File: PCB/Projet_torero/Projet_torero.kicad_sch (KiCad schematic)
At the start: 0 parts

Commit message: Add files via upload
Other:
- added sheet ALIMENTATION (Alimentation.kicad_sch)
- sheet PUISSANCE ports: added FWDD, FWDG, REVD, REVG, V7.2; removed none
- sheet STM32 ports: added FWDD, FWDG, REVD, REVG; removed none
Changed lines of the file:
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@@
 	(generator_version "8.0")
 	(paper "A4")
+	(wire
+		(pts
+			(xy 129.54 63.5) (xy 140.97 63.5)
+		)
+		(stroke
+			(width 0)
+			(type default)
+		)
+	)
+	(wire
+		(pts
+			(xy 129.54 55.88) (xy 140.97 55.88)
+		)
+		(stroke
+			(width 0)
+			(type default)
+		)
+	)
+	(wire
+		(pts
+			(xy 129.54 58.42) (xy 140.97 58.42)
+		)
+		(stroke
+			(width 0)
+			(type default)
+		)
+	)
+	(wire
+		(pts
+			(xy 129.54 60.96) (xy 140.97 60.96)
+		)
+		(stroke
+			(width 0)
+			(type default)
+		)
+	)
 	(sheet
 		(at 22.86 114.3)
@@
 			)
 		)
+		(pin "FWDG" input
+			(at 129.54 55.88 0)
+			(effects
+				(font
+					(size 1.27 1.27)
+				)
+				(justify right)
+			)
+		)
+		(pin "REVG" input
+			(at 129.54 58.42 0)
+			(effects
+				(font
+					(size 1.27 1.27)
+				)
+				(justify right)
+			)
+		)
+		(pin "FWDD" input
+			(at 129.54 60.96 0)
+			(effects
+				(font
+					(size 1.27 1.27)
+				)
+				(justify right)
+			)
+		)
+		(pin "REVD" input
+			(at 129.54 63.5 0)
+			(effects
+				(font
+					(size 1.27 1.27)
+				)
+				(justify right)
+			)
+		)
 		(instances
 			(project "Projet_torero"
@@
 	)
 	(sheet
+		(at 176.53 113.03)
+		(size 83.82 41.91)
+		(fields_autoplaced yes)
+		(stroke
+			(width 0.1524)
+			(type solid)
+		)
+		(fill
+			(color 0 0 0 0.0000)
+		)
+		(property "Sheetname" "ALIMENTATION"
+			(at 176.53 112.3184 0)
+			(effects
+				(font
+					(size 1.27 1.27)
+				)
+				(justify left bottom)
+			)
+		)
+		(property "Sheetfile" "Alimentation.kicad_sch"
+			(at 176.53 155.5246 0)
+			(effects
+				(font
+					(size 1.27 1.27)
+				)
+				(justify left top)
+			)
+		)
+		(instances
+			(project "Projet_torero"
+				(path "/04e1eb47-a2c4-462b-bef7-377d9515a2c0"
+					(page "5")
+				)
+			)
+		)
+	)
+	(sheet
 		(at 140.97 24.13)
 		(size 130.81 72.39)
@@
 			)
 		)
+		(pin "V7.2" input
+			(at 140.97 44.45 180)
+			(effects
+				(font
+					(size 1.27 1.27)
+				)
+				(justify left)
+			)
+		)
+		(pin "REVD" input
+			(at 140.97 63.5 180)
+			(effects
+				(font
+					(size 1.27 1.27)
+				)
+				(justify left)
+			)
+		)
+		(pin "FWDD" input
+			(at 140.97 60.96 180)
+			(effects
+				(font
+					(size 1.27 1.27)
+				)
+				(justify left)
+			)
+		)
+		(pin "REVG" input
+			(at 140.97 58.42 180)
+			(effects
+				(font
+					(size 1.27 1.27)
+				)
+				(justify left)
+			)
+		)
+		(pin "FWDG" input
+			(at 140.97 55.88 180)
+			(effects
+				(font
+					(size 1.27 1.27)
+				)
+				(justify left)
+			)
+		)

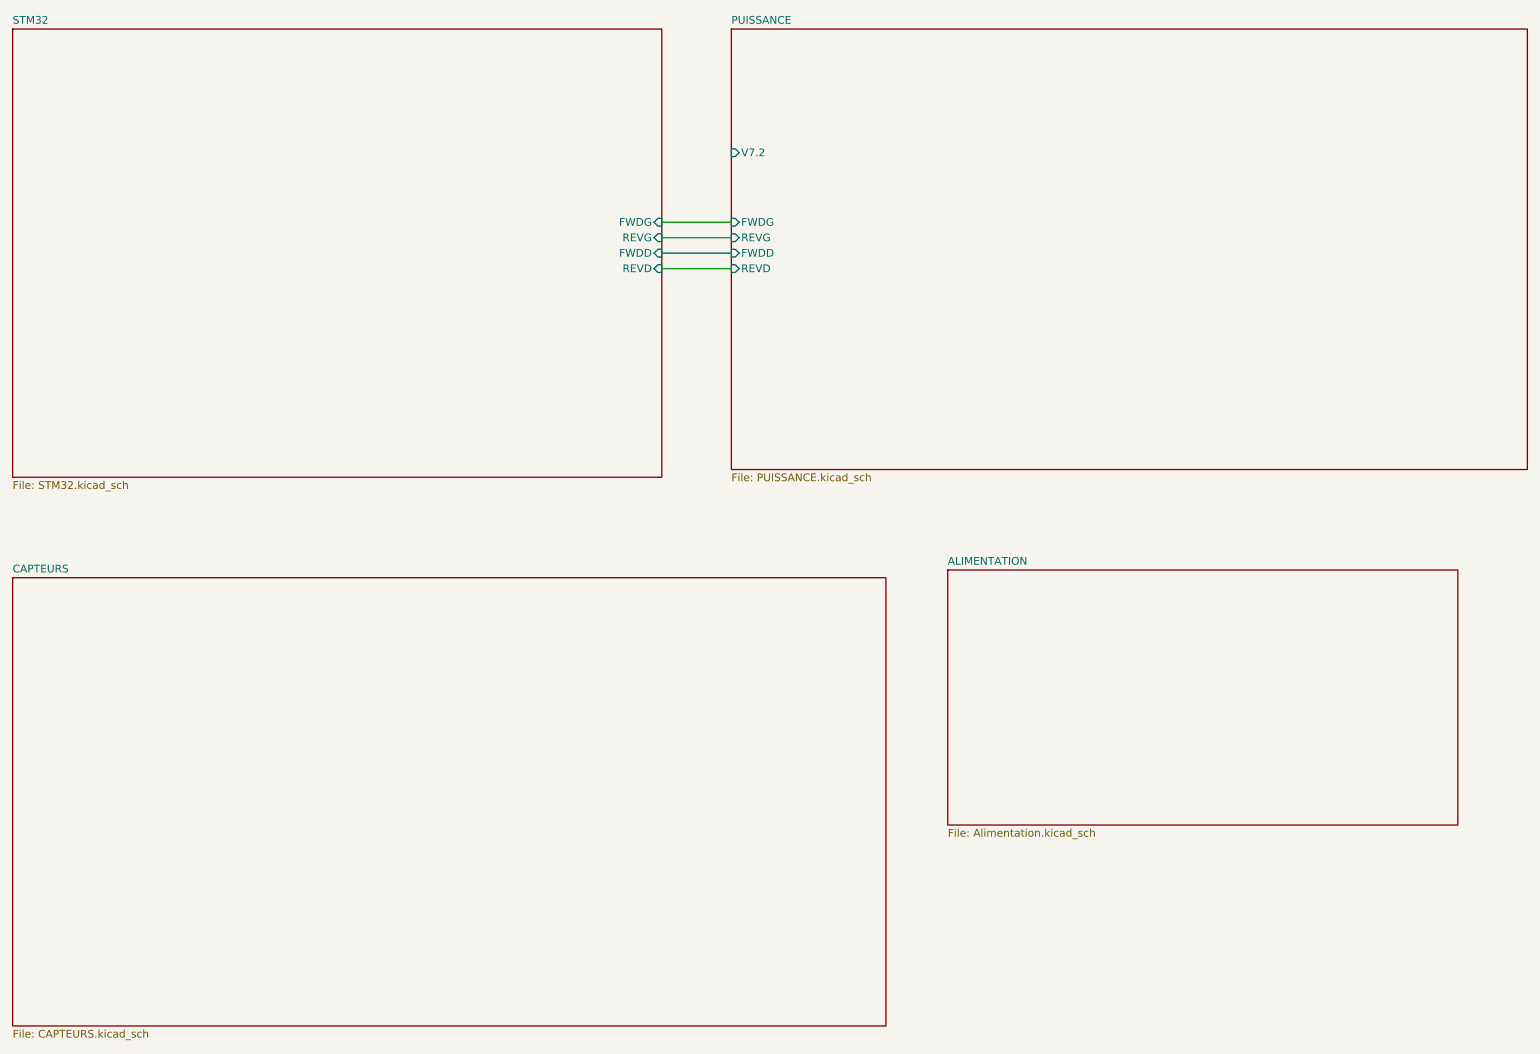
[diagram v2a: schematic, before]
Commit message: Mis à jour, manque l'interupteur ON/OFF
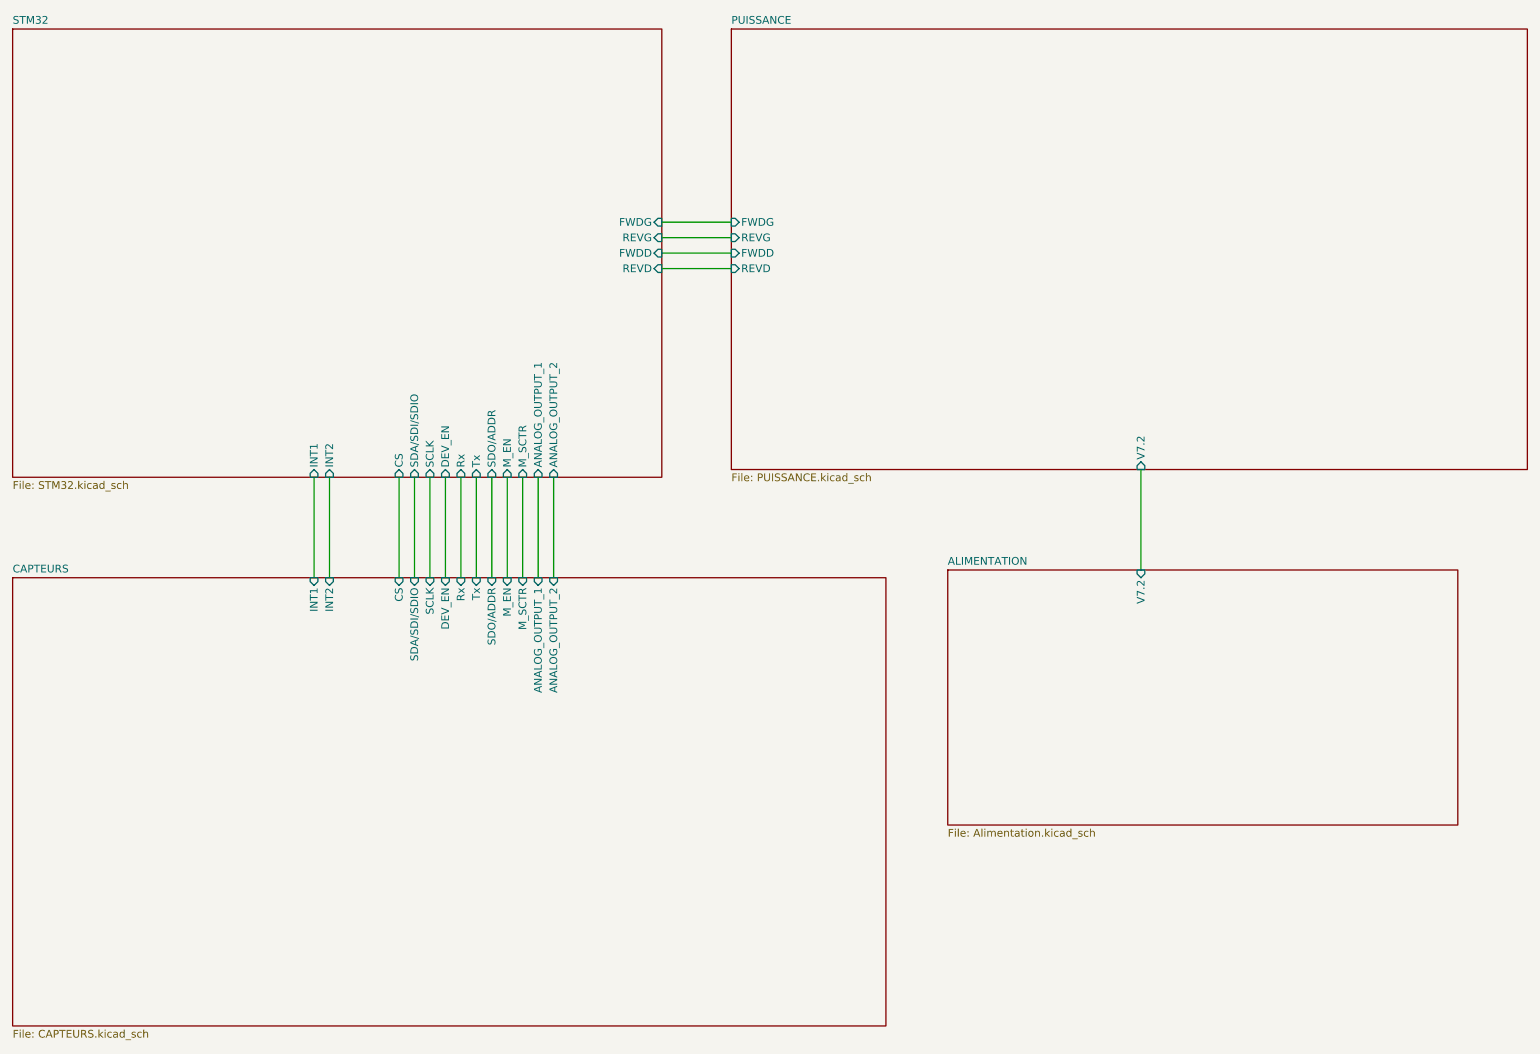
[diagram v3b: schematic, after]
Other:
- sheet ALIMENTATION ports: added V7.2; removed none
- sheet CAPTEURS ports: added ANALOG_OUTPUT_1, ANALOG_OUTPUT_2, CS, DEV_EN, INT1, INT2, M_EN, M_SCTR, Rx, SCLK, SDA/SDI/SDIO, SDO/ADDR, Tx; removed none
- sheet STM32 ports: added ANALOG_OUTPUT_1, ANALOG_OUTPUT_2, CS, DEV_EN, INT1, INT2, M_EN, M_SCTR, Rx, SCLK, SDA/SDI/SDIO, SDO/ADDR, Tx; removed none

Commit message: review sch
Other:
- sheet ALIMENTATION ports: added none; removed V7.2
- sheet CAPTEURS ports: added ANALOG_OUTPUT_CAPT_BORD_D, ANALOG_OUTPUT_CAPT_BORD_G, CS_ACC, DEV_EN_LIDAR, INT1_ACC, INT2_ACC, M_EN_LIDAR, M_SCTR_LIDAR, Rx_LIDAR, SCLK_ACC, SDI_ACC, SDO_ACC, Tx_LIDAR; removed ANALOG_OUTPUT_1, ANALOG_OUTPUT_2, CS, DEV_EN, INT1, INT2, M_EN, M_SCTR, Rx, SCLK, SDA/SDI/SDIO, SDO/ADDR, Tx
- sheet PUISSANCE ports: added EncodeurA_Droite, EncodeurA_Gauche, EncodeurB_Droite, EncodeurB_Gauche; removed V7.2
- sheet STM32 ports: added ANALOG_OUTPUT_CAPT_BORD_D, ANALOG_OUTPUT_CAPT_BORD_G, CS_ACC, DEV_EN_LIDAR, EncodeurA_Droite, EncodeurA_Gauche, EncodeurB_Droite, EncodeurB_Gauche, INT1_ACC, INT2_ACC, M_EN_LIDAR, M_SCTR_LIDAR, Rx_LIDAR, SCLK_ACC, SDI_ACC, SDO_ACC, Tx_LIDAR; removed ANALOG_OUTPUT_1, ANALOG_OUTPUT_2, CS, DEV_EN, INT1, INT2, M_EN, M_SCTR, Rx, SCLK, SDA/SDI/SDIO, SDO/ADDR, Tx
